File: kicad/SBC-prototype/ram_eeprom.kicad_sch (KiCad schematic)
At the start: 2 parts, among them IC3 AT28C256-15PU, IC4 AS6C62256-55PCN

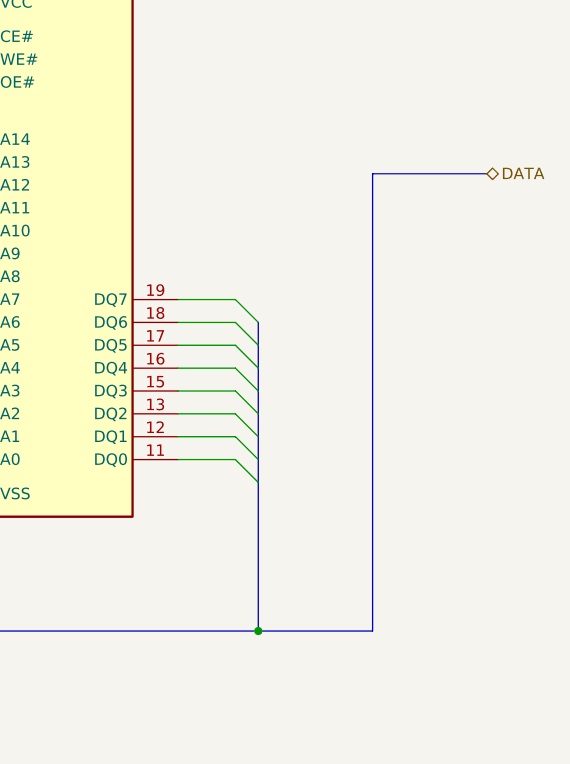
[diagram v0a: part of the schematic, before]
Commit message: Added a power LED, decoupling caps for the power supply and each IC
- Power supply now has a 100uF polarized cap on the 5V rail and 0.1uF
  caps on each of the IC power pins.
- Going to add a VIA to drive an LCD display and then build it
- Haven't looked at footprints yet
- Power input needs a SPDT power switch (I like the power switch like
  what is on the Xilinx FPGA eval boards).
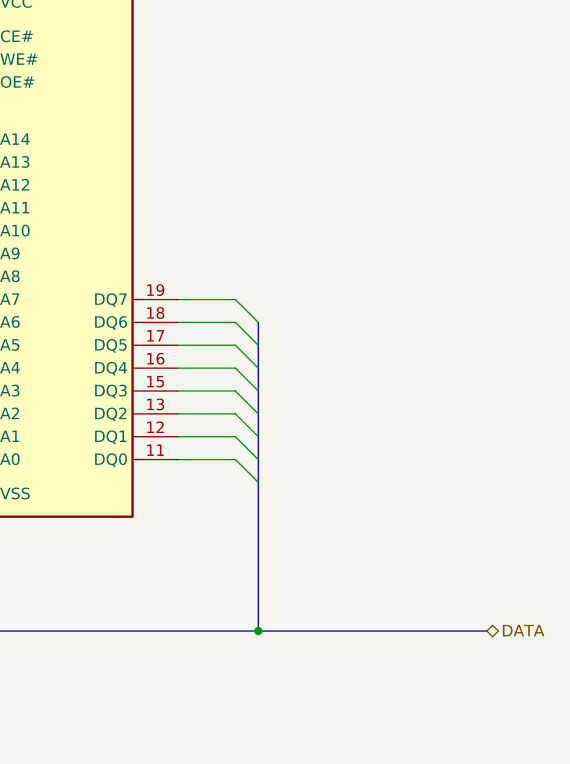
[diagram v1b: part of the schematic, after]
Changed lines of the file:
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@@
 	(bus
 		(pts
-			(xy 222.25 140.97) (xy 234.95 140.97)
+			(xy 222.25 140.97) (xy 247.65 140.97)
 		)
 		(stroke
@@
 	(bus
 		(pts
-			(xy 234.95 140.97) (xy 234.95 90.17)
-		)
-		(stroke
-			(width 0)
-			(type default)
-		)
-	)
-	(bus
-		(pts
 			(xy 138.43 111.76) (xy 138.43 114.3)
 		)
@@
 		(pts
 			(xy 95.25 104.14) (xy 104.14 104.14)
-		)
-		(stroke
-			(width 0)
-			(type default)
-		)
-	)
-	(bus
-		(pts
-			(xy 234.95 90.17) (xy 247.65 90.17)
 		)
 		(stroke
@@
 	(hierarchical_label "DATA"
 		(shape bidirectional)
-		(at 247.65 90.17 0)
+		(at 247.65 140.97 0)
 		(fields_autoplaced yes)
 		(effects

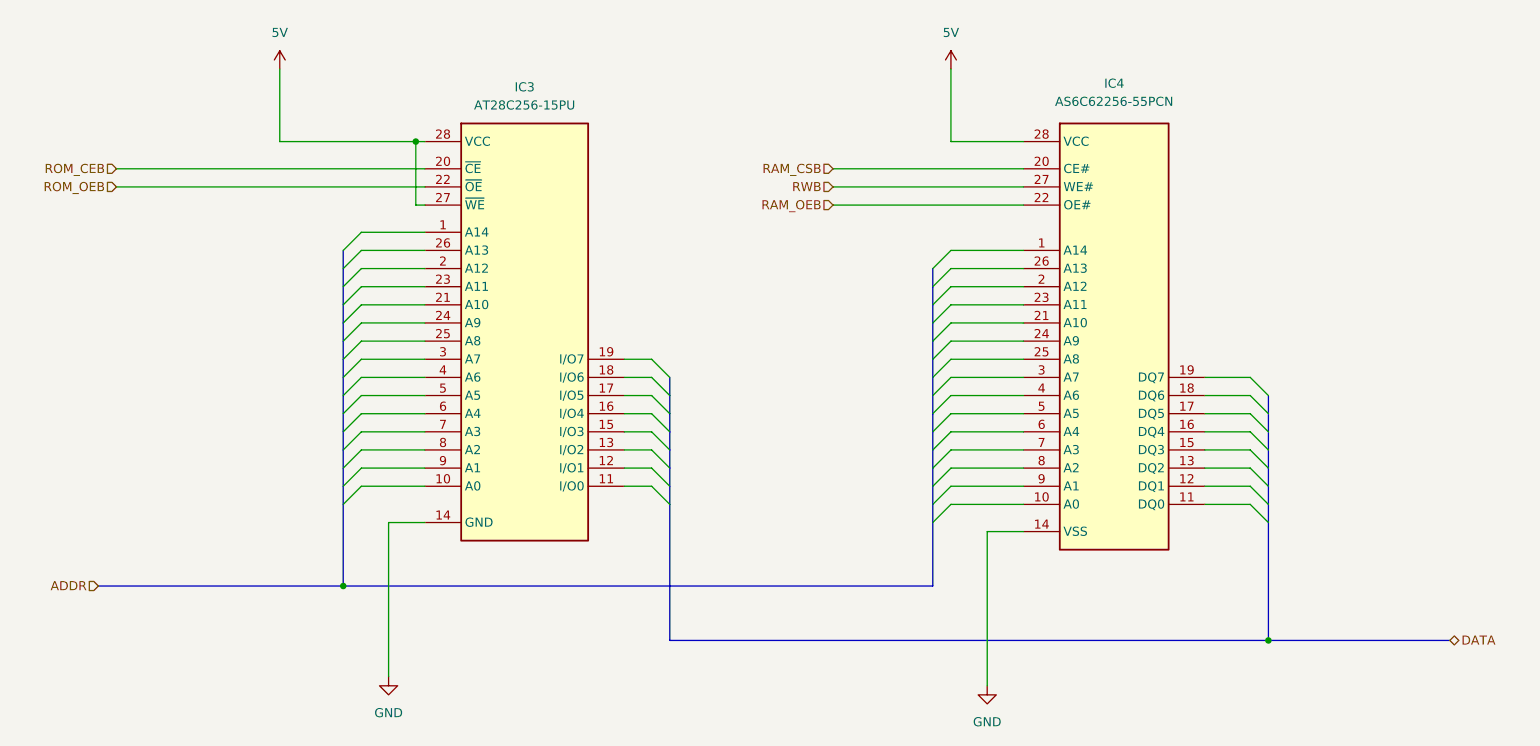
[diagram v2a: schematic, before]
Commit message: Fixed a ton of DRC errors and warnings
- VIA 1 is still unconnected since it's on the breadboard that way and I
  haven't hooked it to anything yet
- All the parts in the library have changed because I've modified my own
  versions of them. I'm not sure if I should add my changes to the
  library or find a way to tell the tool that it's OK that those are
  updated.
- The 74HC00 NAND gate was completely broken and would have been an
  interesting problem to sort out during routing and placement
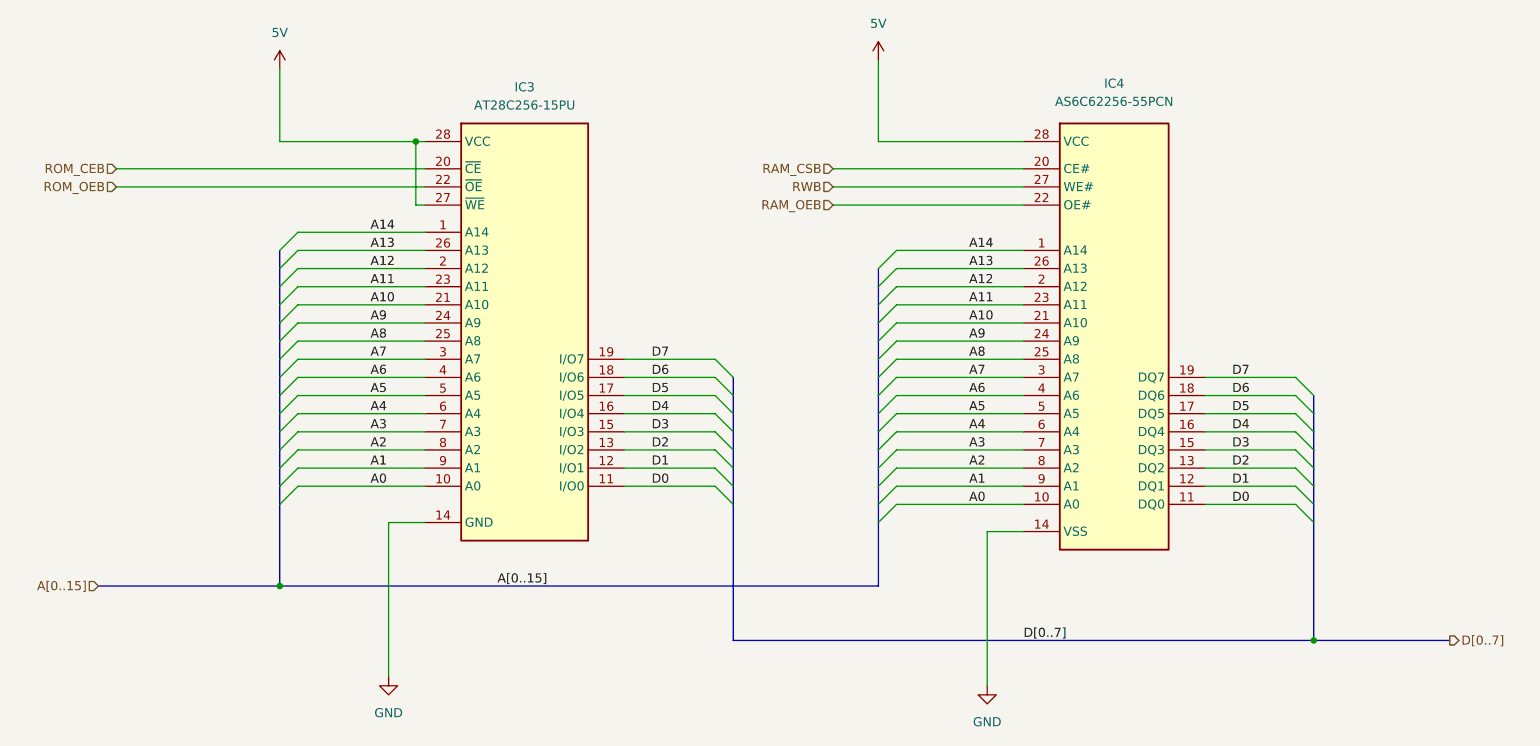
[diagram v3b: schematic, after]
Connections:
- net A14: now reaches IC3.1 (A14)
- net A14: now also IC4.1 (A14)
- net A0: now reaches IC3.10 (A0)
- net A0: now also IC4.10 (A0)
- net D0: now reaches IC3.11 (I/O0)
- net D0: now also IC4.11 (DQ0)
- net D1: now reaches IC3.12 (I/O1)
- net D1: now also IC4.12 (DQ1)
- net D2: now reaches IC3.13 (I/O2)
- net D2: now also IC4.13 (DQ2)
- net D3: now reaches IC3.15 (I/O3)
- net D3: now also IC4.15 (DQ3)
- net D4: now reaches IC3.16 (I/O4)
- net D4: now also IC4.16 (DQ4)
- net D5: now reaches IC3.17 (I/O5)
- net D5: now also IC4.17 (DQ5)
- net D6: now reaches IC3.18 (I/O6)
- net D6: now also IC4.18 (DQ6)
- net D7: now reaches IC3.19 (I/O7)
- net D7: now also IC4.19 (DQ7)
- net A12: now reaches IC3.2 (A12)
- net A12: now also IC4.2 (A12)
- net A10: now reaches IC3.21 (A10)
- net A10: now also IC4.21 (A10)
- net A11: now reaches IC3.23 (A11)
- net A11: now also IC4.23 (A11)
- net A9: now reaches IC3.24 (A9)
- net A9: now also IC4.24 (A9)
- net A8: now reaches IC3.25 (A8)
- net A8: now also IC4.25 (A8)
- net A13: now reaches IC3.26 (A13)
- net A13: now also IC4.26 (A13)
- net A7: now reaches IC3.3 (A7)
- net A7: now also IC4.3 (A7)
- net A6: now reaches IC3.4 (A6)
- net A6: now also IC4.4 (A6)
- net A5: now reaches IC3.5 (A5)
- net A5: now also IC4.5 (A5)
- net A4: now reaches IC3.6 (A4)
- net A4: now also IC4.6 (A4)
- net A3: now reaches IC3.7 (A3)
- net A3: now also IC4.7 (A3)
- net A2: now reaches IC3.8 (A2)
- net A2: now also IC4.8 (A2)
- net A1: now reaches IC3.9 (A1)
- net A1: now also IC4.9 (A1)
